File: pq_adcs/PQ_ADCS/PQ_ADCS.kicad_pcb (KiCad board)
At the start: 4 copper layers, 40 x 40 mm, 53 parts, among them IC2 TMUX1108RSVR, IC3 SN74AUP1G08DBVT, J1 LAT, J3 TOP, J4 SLW-110-01-X-S, J5 SLW-110-01-X-S, J6 SLW-110-01-X-S, J7 SLW-110-01-X-S, J8 LAT, J9 LAT, U1 MMC5983MA, U2 LT6005CDHC#TRPBF, U3 PCA9547BS,118, U5 LT6004IMS8#PBF

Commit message: RIP Stefan in NSL
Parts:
- added H1: MountingHole_Pad, MountingHole:MountingHole_3.2mm_M3_Pad, F.Cu at (83.7, 43.3)
- added H2: MountingHole_Pad, MountingHole:MountingHole_3.2mm_M3_Pad, F.Cu at (116.7, 43.3)
- added H3: MountingHole_Pad, MountingHole:MountingHole_3.2mm_M3_Pad, F.Cu at (116.7, 76.3)
- added H4: MountingHole_Pad, MountingHole:MountingHole_3.2mm_M3_Pad, F.Cu at (83.7, 76.3)
- J1: renamed from J7; value SLW-110-01-X-S -> CES-110-02-L-S
- J1, J8, J9: value LAT -> Conn_01x10_MountingPin
- J2: renamed from J4; value SLW-110-01-X-S -> CES-110-02-L-S
- J3: renamed from J6; value SLW-110-01-X-S -> CES-110-02-L-S
- J3: value TOP -> Conn_01x11_MountingPin
- J4: renamed from J5; value SLW-110-01-X-S -> CES-110-02-L-S
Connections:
- C1 pad 1: (no net) -> GND
- C1 pad 2: (no net) -> /VCC
- C10 pad 1: (no net) -> /ph3_ADCS
- C10 pad 2: (no net) -> Net-(C10-Pad2)
- C11 pad 1: (no net) -> /ph4_ADCS
- C11 pad 2: (no net) -> Net-(C11-Pad2)
- C12 pad 1: (no net) -> Net-(C12-Pad1)
- C12 pad 2: (no net) -> /ph6_ADCS
- C13 pad 1: (no net) -> Net-(C13-Pad1)
- C13 pad 2: (no net) -> /ph5_ADCS
- C14 pad 1: (no net) -> /ph_OBC
- C14 pad 2: (no net) -> GND
- C15 pad 1: (no net) -> /VCC
- C15 pad 2: (no net) -> GND
- C16 pad 1: (no net) -> /VCC
- C16 pad 2: (no net) -> GND
- C2 pad 1: (no net) -> GND
- C2 pad 2: (no net) -> Net-(C2-Pad2)
- C3 pad 1: (no net) -> GND
- C3 pad 2: (no net) -> /VCC
- C4 pad 1: (no net) -> GND
- C4 pad 2: (no net) -> /VCC
- C5 pad 1: (no net) -> GND
- C5 pad 2: (no net) -> /VCC
- C6 pad 1: (no net) -> Net-(C6-Pad1)
- C6 pad 2: (no net) -> GND
- C7 pad 1: (no net) -> /VCC
- C7 pad 2: (no net) -> GND
- C8 pad 1: (no net) -> Net-(C8-Pad1)
- C8 pad 2: (no net) -> /ph1_ADCS
- C9 pad 1: (no net) -> Net-(C9-Pad1)
- C9 pad 2: (no net) -> /ph2_ADCS
- IC2 pad 1: (no net) -> /VCC
- IC2 pad 10: (no net) -> GND
- IC2 pad 11: (no net) -> /VCC
- IC2 pad 12: (no net) -> GND
- IC2 pad 13: (no net) -> /SEL_PH2
- IC2 pad 14: (no net) -> /SEL_PH1
- IC2 pad 15: (no net) -> /SEL_PH0
- IC2 pad 16: (no net) -> Net-(IC2-Pad16)
- IC2 pad 2: (no net) -> GND
- IC2 pad 3: (no net) -> /ph2_ADCS
- IC2 pad 4: (no net) -> /ph3_ADCS
- IC2 pad 5: (no net) -> /ph5_ADCS
- IC2 pad 6: (no net) -> /ph_OBC
- IC2 pad 7: (no net) -> /ph4_ADCS
- IC2 pad 8: (no net) -> /ph1_ADCS
- IC2 pad 9: (no net) -> /ph6_ADCS
- IC3 pad 1: (no net) -> /SEL_PH0
- IC3 pad 2: (no net) -> /SEL_PH1
- IC3 pad 3: (no net) -> GND
- IC3 pad 4: (no net) -> Net-(IC2-Pad16)
- IC3 pad 5: (no net) -> /VCC
- J1 pad 1: (no net) -> /SDA
- J1 pad 10: (no net) -> /VCC
- J1 pad 2: (no net) -> /SCL
- J1 pad 3: (no net) -> unconnected-(J7-Pad3)
- J1 pad 4: (no net) -> /BATT++
- J1 pad 5: (no net) -> unconnected-(J7-Pad5)
- J1 pad 6: (no net) -> unconnected-(J7-Pad6)
- J1 pad 7: (no net) -> unconnected-(J7-Pad7)
- J1 pad 8: (no net) -> unconnected-(J7-Pad8)
- J1 pad 9: (no net) -> GND
- J1 pad 1: (no net) -> /SOLAR_X
- J1 pad 10: (no net) -> GND
- J1 pad 2: (no net) -> GND
- J1 pad 3: (no net) -> /Iout6
- J1 pad 4: (no net) -> /VCC
- J1 pad 5: (no net) -> /SDA
- J1 pad 6: (no net) -> /SCL
- J1 pad 7: (no net) -> GND
- J1 pad 8: (no net) -> /pht6
- J1 pad 9: (no net) -> /BURNCOMMS
- J2 pad 1: (no net) -> unconnected-(J4-Pad1)
- J2 pad 10: (no net) -> unconnected-(J4-Pad10)
- J2 pad 2: (no net) -> unconnected-(J4-Pad2)
- J2 pad 3: (no net) -> unconnected-(J4-Pad3)
- J2 pad 4: (no net) -> /SOLAR_Y
- J2 pad 5: (no net) -> /SEL_PH0
- J2 pad 6: (no net) -> /SEL_PH1
- J2 pad 7: (no net) -> unconnected-(J4-Pad7)
- J2 pad 8: (no net) -> unconnected-(J4-Pad8)
- J2 pad 9: (no net) -> /BURNCOMMS
- J3 pad 1: (no net) -> unconnected-(J6-Pad1)
- J3 pad 10: (no net) -> /SOLAR_Z
- J3 pad 2: (no net) -> unconnected-(J6-Pad2)
- J3 pad 3: (no net) -> /VStef
- J3 pad 4: (no net) -> unconnected-(J6-Pad4)
- J3 pad 5: (no net) -> /SEL_PH2
- J3 pad 6: (no net) -> /ph_OBC
- J3 pad 7: (no net) -> /RST_Drivers
- J3 pad 8: (no net) -> unconnected-(J6-Pad8)
- J3 pad 9: (no net) -> unconnected-(J6-Pad9)
- J3 pad 1: (no net) -> /VStef
- J3 pad 10: (no net) -> /Iout1
- J3 pad 11: (no net) -> GND
- J3 pad 2: (no net) -> /SWCLK
- J3 pad 3: (no net) -> /SWDIO
- J3 pad 4: (no net) -> /VCC
- J3 pad 5: (no net) -> /SDA
- J3 pad 6: (no net) -> /SCL
- J3 pad 7: (no net) -> GND
- J3 pad 8: (no net) -> /pht3
- J3 pad 9: (no net) -> GND
- J4 pad 1: (no net) -> unconnected-(J5-Pad1)
- J4 pad 10: (no net) -> /SOLAR_X
- J4 pad 2: (no net) -> unconnected-(J5-Pad2)
- J4 pad 3: (no net) -> unconnected-(J5-Pad3)
- J4 pad 4: (no net) -> /SWCLK
- J4 pad 5: (no net) -> /SWDIO
- J4 pad 6: (no net) -> /NRST
- J4 pad 7: (no net) -> unconnected-(J5-Pad7)
- J4 pad 8: (no net) -> unconnected-(J5-Pad8)
- J4 pad 9: (no net) -> unconnected-(J5-Pad9)
- J8 pad 1: (no net) -> /SOLAR_Z
- J8 pad 10: (no net) -> GND
- J8 pad 2: (no net) -> GND
- J8 pad 3: (no net) -> /Iout5
- J8 pad 4: (no net) -> /VCC
- J8 pad 5: (no net) -> /SDA
- J8 pad 6: (no net) -> /SCL
- J8 pad 7: (no net) -> GND
- J8 pad 8: (no net) -> /pht5
- J8 pad 9: (no net) -> /BURNCOMMS
- J9 pad 1: (no net) -> /SOLAR_Z
- J9 pad 10: (no net) -> GND
- J9 pad 2: (no net) -> GND
- J9 pad 3: (no net) -> /Iout4
- J9 pad 4: (no net) -> /VCC
- J9 pad 5: (no net) -> /SDA
- J9 pad 6: (no net) -> /SCL
- J9 pad 7: (no net) -> GND
- J9 pad 8: (no net) -> /pht1
- J9 pad 9: (no net) -> /BURNCOMMS
- LV1CT1 pad A1: (no net) -> /SCL1
- LV1CT1 pad A2: (no net) -> /NRST
- LV1CT1 pad B1: (no net) -> /SDA1
- LV1CT1 pad B2: (no net) -> /VCC
- LV1CT1 pad C1: (no net) -> GND
- LV1CT1 pad C2: (no net) -> /Iout1
- LV2CT1 pad A1: (no net) -> /SCL2
- LV2CT1 pad A2: (no net) -> /NRST
- LV2CT1 pad B1: (no net) -> /SDA2
- LV2CT1 pad B2: (no net) -> /VCC
- LV2CT1 pad C1: (no net) -> GND
- LV2CT1 pad C2: (no net) -> /Iout2
- LV3CT1 pad A1: (no net) -> /SCL3
- LV3CT1 pad A2: (no net) -> /NRST
- LV3CT1 pad B1: (no net) -> /SDA3
- LV3CT1 pad B2: (no net) -> /VCC
- LV3CT1 pad C1: (no net) -> GND
- LV3CT1 pad C2: (no net) -> /Iout3
- LV4CT1 pad A1: (no net) -> /SCL4
- LV4CT1 pad A2: (no net) -> /NRST
- LV4CT1 pad B1: (no net) -> /SDA4
- LV4CT1 pad B2: (no net) -> /VCC
- LV4CT1 pad C1: (no net) -> GND
- LV4CT1 pad C2: (no net) -> /Iout4
- LV5CT1 pad A1: (no net) -> /SCL5
- LV5CT1 pad A2: (no net) -> /NRST
- LV5CT1 pad B1: (no net) -> /SDA5
- LV5CT1 pad B2: (no net) -> /VCC
- LV5CT1 pad C1: (no net) -> GND
- LV5CT1 pad C2: (no net) -> /Iout5
- LV6CT1 pad A1: (no net) -> /SCL6
- LV6CT1 pad A2: (no net) -> /NRST
- LV6CT1 pad B1: (no net) -> /SDA6
- LV6CT1 pad B2: (no net) -> /VCC
- LV6CT1 pad C1: (no net) -> GND
- LV6CT1 pad C2: (no net) -> /Iout6
- R1 pad 1: (no net) -> /pht1
- R1 pad 2: (no net) -> Net-(C8-Pad1)
- R10 pad 1: (no net) -> Net-(C11-Pad2)
- R10 pad 2: (no net) -> /ph4_ADCS
- R11 pad 1: (no net) -> Net-(C11-Pad2)
- R11 pad 2: (no net) -> /pht4
- R12 pad 1: (no net) -> /ph6_ADCS
- R12 pad 2: (no net) -> Net-(C12-Pad1)
- R13 pad 1: (no net) -> /ph5_ADCS
- R13 pad 2: (no net) -> Net-(C13-Pad1)
- R14 pad 1: (no net) -> Net-(C12-Pad1)
- R14 pad 2: (no net) -> /pht6
- R15 pad 1: (no net) -> Net-(C13-Pad1)
- R15 pad 2: (no net) -> /pht5
- R2 pad 1: (no net) -> /ph1_ADCS
- R2 pad 2: (no net) -> Net-(C8-Pad1)
- R3 pad 1: (no net) -> /VCC
- R3 pad 10: (no net) -> GND
- R3 pad 11: (no net) -> GND
- R3 pad 12: (no net) -> GND
- R3 pad 13: (no net) -> GND
- R3 pad 14: (no net) -> Net-(C2-Pad2)
- R3 pad 15: (no net) -> GND
- R3 pad 16: (no net) -> /VCC
- R3 pad 2: (no net) -> /SCL
- R3 pad 3: (no net) -> /SDA
- R3 pad 4: (no net) -> unconnected-(R3-Pad4)
- R3 pad 5: (no net) -> /VCC
- R3 pad 6: (no net) -> unconnected-(R3-Pad6)
- R3 pad 7: (no net) -> unconnected-(R3-Pad7)
- R3 pad 8: (no net) -> GND
- R3 pad 9: (no net) -> GND
- R4 pad 1: (no net) -> /SCL
- R4 pad 2: (no net) -> /VCC
- R5 pad 1: (no net) -> /VCC
- R5 pad 2: (no net) -> /SDA
- R6 pad 1: (no net) -> /ph2_ADCS
- R6 pad 2: (no net) -> Net-(C9-Pad1)
- R7 pad 1: (no net) -> Net-(C10-Pad2)
- R7 pad 2: (no net) -> /ph3_ADCS
- R8 pad 1: (no net) -> Net-(C10-Pad2)
- R8 pad 2: (no net) -> /pht3
- R9 pad 1: (no net) -> /pht2
- R9 pad 2: (no net) -> Net-(C9-Pad1)
- U1 pad 1: (no net) -> /SCL
- U1 pad 10: (no net) -> Net-(C6-Pad1)
- U1 pad 11: (no net) -> GND
- U1 pad 12: (no net) -> unconnected-(U1-Pad12)
- U1 pad 13: (no net) -> /VCC
- U1 pad 14: (no net) -> unconnected-(U1-Pad14)
- U1 pad 15: (no net) -> unconnected-(U1-Pad15)
- U1 pad 16: (no net) -> /SDA
- U1 pad 2: (no net) -> /VCC
- U1 pad 3: (no net) -> unconnected-(U1-Pad3)
- U1 pad 4: (no net) -> /VCC
- U1 pad 5: (no net) -> unconnected-(U1-Pad5)
- U1 pad 6: (no net) -> unconnected-(U1-Pad6)
- U1 pad 7: (no net) -> unconnected-(U1-Pad7)
- U1 pad 8: (no net) -> unconnected-(U1-Pad8)
- U1 pad 9: (no net) -> GND
- U2 pad 1: (no net) -> /ph1_ADCS
- U2 pad 10: (no net) -> /ph4_ADCS
- U2 pad 11: (no net) -> Net-(C11-Pad2)
- U2 pad 12: (no net) -> GND
- U2 pad 13: (no net) -> GND
- U2 pad 14: (no net) -> GND
- U2 pad 15: (no net) -> Net-(C10-Pad2)
- U2 pad 16: (no net) -> /ph3_ADCS
- U2 pad 17: (no net) -> unconnected-(U2-Pad17)
- U2 pad 2: (no net) -> Net-(C8-Pad1)
- U2 pad 3: (no net) -> GND
- U2 pad 4: (no net) -> /VCC
- U2 pad 5: (no net) -> GND
- U2 pad 6: (no net) -> Net-(C9-Pad1)
- U2 pad 7: (no net) -> /ph2_ADCS
- U2 pad 8: (no net) -> unconnected-(U2-Pad8)
- U2 pad 9: (no net) -> unconnected-(U2-Pad9)
- U3 pad 1: (no net) -> /SDA1
- U3 pad 10: (no net) -> /SDA5
- U3 pad 11: (no net) -> /SCL5
- U3 pad 12: (no net) -> /SDA6
- U3 pad 13: (no net) -> /SCL6
- U3 pad 14: (no net) -> unconnected-(U3-Pad14)
- U3 pad 15: (no net) -> unconnected-(U3-Pad15)
- U3 pad 16: (no net) -> unconnected-(U3-Pad16)
- U3 pad 17: (no net) -> unconnected-(U3-Pad17)
- U3 pad 18: (no net) -> GND
- U3 pad 19: (no net) -> /SCL
- U3 pad 2: (no net) -> /SCL1
- U3 pad 20: (no net) -> /SDA
- U3 pad 21: (no net) -> /VCC
- U3 pad 22: (no net) -> GND
- U3 pad 23: (no net) -> GND
- U3 pad 24: (no net) -> /RST_Drivers
- U3 pad 25: (no net) -> unconnected-(U3-Pad25)
- U3 pad 3: (no net) -> /SDA2
- U3 pad 4: (no net) -> /SCL2
- U3 pad 5: (no net) -> /SDA3
- U3 pad 6: (no net) -> /SCL3
- U3 pad 7: (no net) -> /SDA4
- U3 pad 8: (no net) -> /SCL4
- U3 pad 9: (no net) -> GND
- U5 pad 1: (no net) -> /ph5_ADCS
- U5 pad 2: (no net) -> Net-(C13-Pad1)
- U5 pad 3: (no net) -> GND
- U5 pad 4: (no net) -> GND
- U5 pad 5: (no net) -> GND
- U5 pad 6: (no net) -> Net-(C12-Pad1)
- U5 pad 7: (no net) -> /ph6_ADCS
- U5 pad 8: (no net) -> /VCC
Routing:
- net (no net): track 1529.1 -> 0.00 mm, vias 83 -> 0
- net GND: track 0.00 -> 265.9 mm, vias 0 -> 25
- net /VCC: track 0.00 -> 164.6 mm, vias 0 -> 3
- net /SCL: track 0.00 -> 94.7 mm, vias 0 -> 5
- net /SDA: track 0.00 -> 89.6 mm, vias 0 -> 4
- net /SOLAR_Z: track 0.00 -> 65.7 mm, vias 0 -> 1
- net /BURNCOMMS: track 0.00 -> 60.4 mm, vias 0 -> 2
- net /SOLAR_X: track 0.00 -> 59.8 mm, vias 0 -> 3
- net /Iout5: track 0.00 -> 50.8 mm, vias 0 -> 2
- net /SOLAR_Y: track 0.00 -> 44.7 mm
- net /VStef: track 0.00 -> 44.3 mm, vias 0 -> 1
- net /Iout4: track 0.00 -> 41.8 mm, vias 0 -> 3
- net /NRST: track 0.00 -> 36.7 mm, vias 0 -> 5
- net /Iout6: track 0.00 -> 34.2 mm, vias 0 -> 2
- net /ph3_ADCS: track 0.00 -> 33.4 mm
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
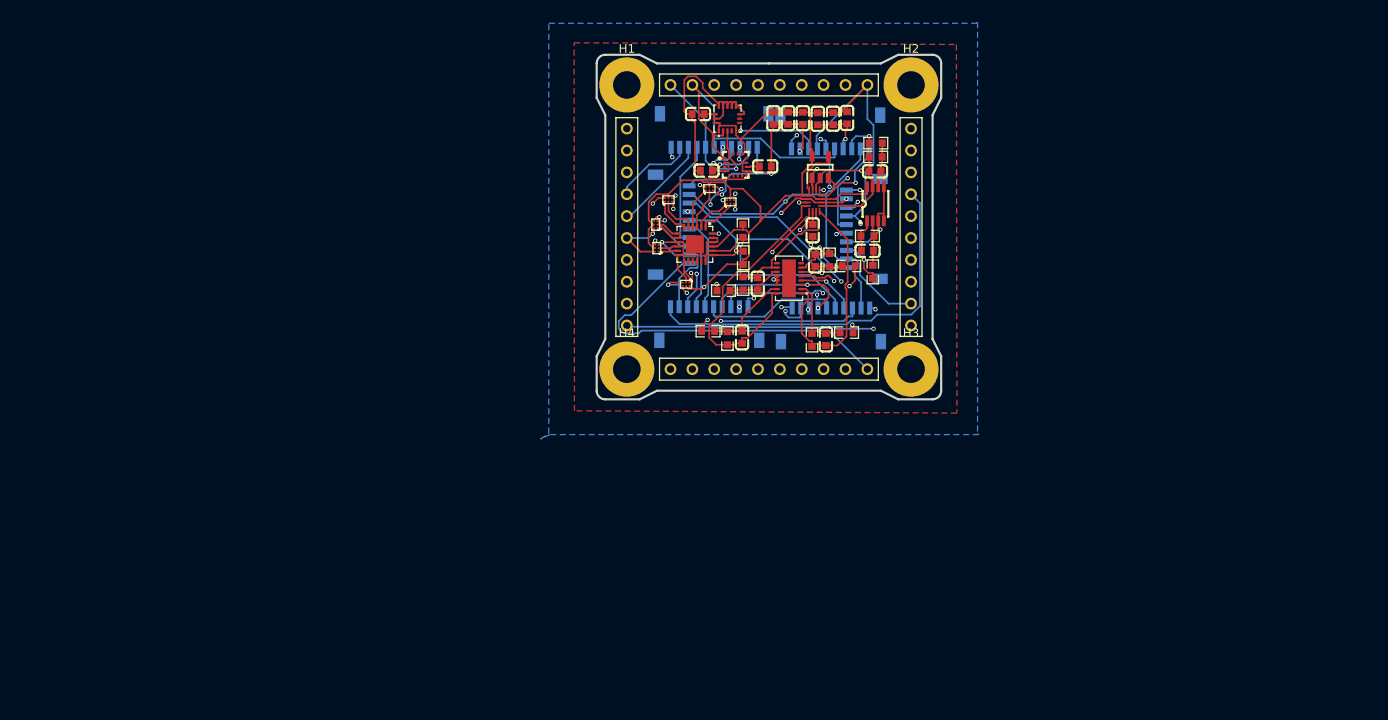
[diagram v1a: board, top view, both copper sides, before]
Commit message: lateral boards added, ADCS schematic lacks mtq drivers
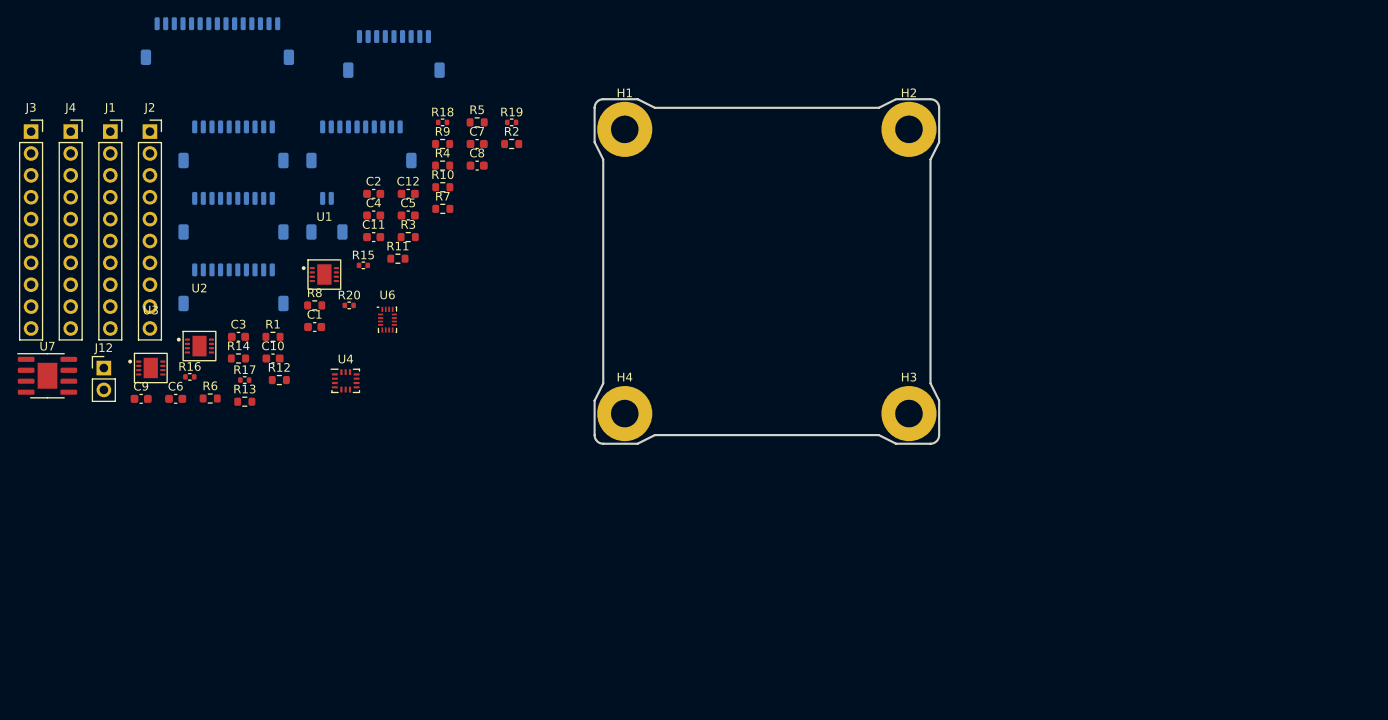
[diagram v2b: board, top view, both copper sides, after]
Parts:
- removed BOT: BOT, easyeda:2023961007
- removed C1: 10nF, easyeda:C0603
- removed C13: 0.1n, easyeda:C0603
- removed C14, C15: 1uF, easyeda:C0603
- removed C16: 1u, easyeda:C0603
- removed the C3 at (105.9, 47.3)
- removed IC2: TMUX1108RSVR, easyeda:QFN40P180X260X55-16N
- removed IC3: SN74AUP1G08DBVT, easyeda:SOT95P280X145-5N
- removed the J1 at (88.8, 43.3)
- removed the J1 at (107.4, 48.1)
- removed the J3 at (88.8, 76.3)
- removed the J3 at (93.9, 47.8)
- removed LAT_: LAT, easyeda:2023961007
- removed LV1CT1, LV2CT1, LV3CT1, LV4CT1, LV5CT1, LV6CT1: LV8498CT_footprint, easyeda:WLP-6_L1.30-W0.90-P0.40-TL
- removed U1: MMC5983MA, easyeda:LGA-16_L3.0-W3.0-P0.50-BL_SQ
- removed the U3 at (91.6, 61.8)
- removed U5: LT6004IMS8#PBF, easyeda:MOSP-8_L3.0-W3.0-P0.65-LS4.9-BL
- added C3: 100 pF, Capacitor_SMD:C_0603_1608Metric, F.Cu at (38.6, 72.6)
- added C3: 100 pF, Capacitor_SMD:C_0603_1608Metric, F.Cu at (47.5, 71.5)
- added J1: CES-110-02-L-S, Connector_PinSocket_2.54mm:PinSocket_1x10_P2.54mm_Vertical, F.Cu at (23.8, 48.8)
- added J10: Pico-Clasp_01x09, Connector_Molex:Molex_Pico-Clasp_202396-0907_1x09-1MP_P1.00mm_Horizontal, B.Cu at (56.7, 39.8)
- added J11: Pico-Clasp_01x15, Connector_Molex:Molex_Pico-Clasp_202396-1507_1x15-1MP_P1.00mm_Horizontal, B.Cu at (36.2, 38.3)
- added J12: CES-102-02-L-S, Connector_PinHeader_2.54mm:PinHeader_1x02_P2.54mm_Vertical, F.Cu at (23.0, 76.2)
- added J3: CES-110-02-L-S, Connector_PinSocket_2.54mm:PinSocket_1x10_P2.54mm_Vertical, F.Cu at (14.6, 48.8)
- added J5: Pico-Clasp_01x02, Connector_Molex:Molex_Pico-Clasp_202396-0207_1x02-1MP_P1.00mm_Horizontal, B.Cu at (48.9, 58.5)
- added J6: Pico-Clasp_01x10, Connector_Molex:Molex_Pico-Clasp_202396-1007_1x10-1MP_P1.00mm_Horizontal, B.Cu at (38.1, 66.8)
- added J7: Pico-Clasp_01x10, Connector_Molex:Molex_Pico-Clasp_202396-1007_1x10-1MP_P1.00mm_Horizontal, B.Cu at (38.1, 58.5)
- added R16: 0R, Resistor_SMD:R_0402_1005Metric, F.Cu at (33.0, 77.2)
- added R17: 0R, Resistor_SMD:R_0402_1005Metric, F.Cu at (39.4, 77.6)
- added R18: 0R, Resistor_SMD:R_0402_1005Metric, F.Cu at (62.4, 47.7)
- added R19: 0R, Resistor_SMD:R_0402_1005Metric, F.Cu at (70.4, 47.7)
- added R20: 0R, Resistor_SMD:R_0402_1005Metric, F.Cu at (51.5, 68.9)
- added U3: LPV542, GGS_Miscellaneous:TI_X1SON-8_3x3mm, F.Cu at (48.6, 65.4)
- added U3: LPV542, GGS_Miscellaneous:TI_X1SON-8_3x3mm, F.Cu at (28.5, 76.2)
- added U4: IIM-42652, Package_LGA:Bosch_LGA-14_3x2.5mm_P0.5mm, F.Cu at (51.1, 77.7)
- added U6: TMUX1108RSVR, GGS_Miscellaneous:UQFN-16_1.8x2.6_Pitch0.4mm, F.Cu at (56.0, 70.6)
- added U7: TCN75AVOA713, Package_SO:SOIC-8-1EP_3.9x4.9mm_P1.27mm_EP2.29x3mm, F.Cu at (16.5, 77.1)
- C10: value 0.1n -> 10 nF; footprint easyeda:C0603 -> Capacitor_SMD:C_0603_1608Metric
- C11, C12, C9: value 0.1n -> 100 nF; footprint easyeda:C0603 -> Capacitor_SMD:C_0603_1608Metric
- C2, C4: value 0.47uF -> 100 pF; footprint easyeda:C0603 -> Capacitor_SMD:C_0603_1608Metric
- C5: value 1uF -> 100 pF; footprint easyeda:C0603 -> Capacitor_SMD:C_0603_1608Metric
- C6: value 10u -> 100 pF; footprint easyeda:C0603 -> Capacitor_SMD:C_0603_1608Metric
- C7: value 0.1u -> 1 uF; footprint easyeda:C0603 -> Capacitor_SMD:C_0603_1608Metric
- C8: value 0.1n -> 2.2 uF; footprint easyeda:C0603 -> Capacitor_SMD:C_0603_1608Metric
- J2, J4: footprint easyeda:SLW-110-01-X-S -> Connector_PinSocket_2.54mm:PinSocket_1x10_P2.54mm_Vertical
- J8, J9: value Conn_01x10_MountingPin -> Pico-Clasp_01x10; footprint easyeda:2023961007 -> Connector_Molex:Molex_Pico-Clasp_202396-1007_1x10-1MP_P1.00mm_Horizontal; moved to B.Cu
- R1, R9: value 100R -> 100; footprint easyeda:R0603 -> Resistor_SMD:R_0603_1608Metric
- R10, R2, R6: value 2k -> 100; footprint easyeda:R0603 -> Resistor_SMD:R_0603_1608Metric
- R11, R8: value 100R -> 2k; footprint easyeda:R0603 -> Resistor_SMD:R_0603_1608Metric
- R12, R7: footprint easyeda:R0603 -> Resistor_SMD:R_0603_1608Metric
- R13: value 2k -> 5k; footprint easyeda:R0603 -> Resistor_SMD:R_0603_1608Metric
- R14: value 100R -> 5k; footprint easyeda:R0603 -> Resistor_SMD:R_0603_1608Metric
- R15: value 100R -> 0R; footprint easyeda:R0603 -> Resistor_SMD:R_0402_1005Metric
- R3: value ICG-20330 -> 2k; footprint easyeda:LGA-16_L3.0-W3.0-P0.50-BL -> Resistor_SMD:R_0603_1608Metric
- R4: value 2.7K -> 2k; footprint easyeda:R0603 -> Resistor_SMD:R_0603_1608Metric
- R5: value 2.7K -> 100; footprint easyeda:R0603 -> Resistor_SMD:R_0603_1608Metric
- U2: value LT6005CDHC#TRPBF -> LPV542; footprint easyeda:DFN-16_L5.0-W3.0-P0.50-BL-EP -> GGS_Miscellaneous:TI_X1SON-8_3x3mm
- moved J2 88.4 mm to (28.4, 48.8), turned to 0 degrees
- moved C9 79.9 mm to (27.4, 79.8), turned to 0 degrees
- moved R14 78.1 mm to (38.6, 75.1), turned to 0 degrees
- moved R13 74.8 mm to (39.4, 80.1)
- moved R12 73.9 mm to (43.4, 77.6)
- moved R6 73.7 mm to (35.4, 79.8), turned to 0 degrees
- moved C6 73.6 mm to (31.4, 79.8)
- moved J9 72.7 mm to (38.1, 50.2), turned to 180 degrees
- moved U2 68.9 mm to (34.1, 73.7), turned to 0 degrees
- moved R1 66.6 mm to (42.7, 72.6), turned to 0 degrees
- moved J4 64.6 mm to (19.2, 48.8), turned to 0 degrees
- moved J8 59.8 mm to (52.9, 50.2), turned to 180 degrees
- moved R15 59.2 mm to (53.1, 64.3), turned to 0 degrees
- moved C4 56.1 mm to (54.4, 58.5), turned to 0 degrees
- moved C10 54.5 mm to (42.7, 75.1), turned to 0 degrees
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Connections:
- net /SOLAR_Z renamed SOLAR_Z
- C10 pad 1: /ph3_ADCS -> 3V3_PERM
- C10 pad 2: Net-(C10-Pad2) -> GND
- C11 pad 1: /ph4_ADCS -> ADCS_POWER
- C11 pad 2: Net-(C11-Pad2) -> GND
- C12 pad 1: Net-(C12-Pad1) -> 3V3_PERM
- C12 pad 2: /ph6_ADCS -> GND
- C2 pad 1: GND -> Net-(C2-Pad1)
- C2 pad 2: Net-(C2-Pad2) -> /PHT2_ADCS
- C4 pad 1: GND -> Net-(C4-Pad1)
- C4 pad 2: /VCC -> /PHT4_ADCS
- C5 pad 1: GND -> /PHT5_ADCS
- C5 pad 2: /VCC -> Net-(C5-Pad2)
- C6 pad 2: GND -> /PHT6_ADCS
- C7 pad 1: /VCC -> 3V3_PERM
- C8 pad 1: Net-(C8-Pad1) -> 3V3_PERM
- C8 pad 2: /ph1_ADCS -> GND
- C9 pad 1: Net-(C9-Pad1) -> 3V3_PERM
- C9 pad 2: /ph2_ADCS -> GND
- J2 pad 1: unconnected-(J4-Pad1) -> STM32_PA15
- J2 pad 10: unconnected-(J4-Pad10) -> GND
- J2 pad 2: unconnected-(J4-Pad2) -> STM32_PB3
- J2 pad 3: unconnected-(J4-Pad3) -> BATT_NTC
- J2 pad 4: /SOLAR_Y -> SOLAR_Y
- J2 pad 5: /SEL_PH0 -> SEL_PH2
- J2 pad 6: /SEL_PH1 -> SEL_PH1
- J2 pad 7: unconnected-(J4-Pad7) -> HEATER_EN
- J2 pad 8: unconnected-(J4-Pad8) -> HEATER_PWR
- J2 pad 9: /BURNCOMMS -> BURNCOMMS
- J4 pad 1: unconnected-(J5-Pad1) -> SOLAR_X
- J4 pad 10: /SOLAR_X -> SCL3
- J4 pad 2: unconnected-(J5-Pad2) -> CHRGOFF
- J4 pad 3: unconnected-(J5-Pad3) -> CLPROG
- J4 pad 4: /SWCLK -> SDA3
- J4 pad 5: /SWDIO -> NRST
- J4 pad 6: /NRST -> SWDIO
- J4 pad 7: unconnected-(J5-Pad7) -> SWCLK
- J4 pad 8: unconnected-(J5-Pad8) -> DAC_PL
- J4 pad 9: unconnected-(J5-Pad9) -> ADC_PL
- J8 pad 10: GND -> BURNCOMMS
- J8 pad 3: /Iout5 -> /MAG-Z
- J8 pad 4: /VCC -> GND
- J8 pad 5: /SDA -> /VCC
- J8 pad 6: /SCL -> /SDA
- J8 pad 7: GND -> /SCL
- J8 pad 8: /pht5 -> /PHT3
- J8 pad 9: /BURNCOMMS -> GND
- J9 pad 10: GND -> BURNCOMMS
- J9 pad 3: /Iout4 -> /MAG+Z
- J9 pad 4: /VCC -> GND
- J9 pad 5: /SDA -> /VCC
- J9 pad 6: /SCL -> /SDA
- J9 pad 7: GND -> /SCL
- J9 pad 8: /pht1 -> /PHT4
- J9 pad 9: /BURNCOMMS -> GND
- R1 pad 1: /pht1 -> /PHT1
- R1 pad 2: Net-(C8-Pad1) -> Net-(C1-Pad2)
- R10 pad 1: Net-(C11-Pad2) -> /PHT6
- R10 pad 2: /ph4_ADCS -> Net-(C6-Pad1)
- R11 pad 1: Net-(C11-Pad2) -> Net-(C5-Pad2)
- R11 pad 2: /pht4 -> /PHT5_ADCS
- R12 pad 1: /ph6_ADCS -> /PHT6_ADCS
- R12 pad 2: Net-(C12-Pad1) -> Net-(C6-Pad1)
- R13 pad 1: /ph5_ADCS -> /SCL
- R13 pad 2: Net-(C13-Pad1) -> 3V3_PERM
- R14 pad 1: Net-(C12-Pad1) -> /SDA
- R14 pad 2: /pht6 -> 3V3_PERM
- R15 pad 1: Net-(C13-Pad1) -> Net-(R15-Pad1)
- R15 pad 2: /pht5 -> 3V3_PERM
- R2 pad 1: /ph1_ADCS -> /PHT2
- R2 pad 2: Net-(C8-Pad1) -> Net-(C2-Pad1)
- R3 pad 1: /VCC -> Net-(C1-Pad2)
- R3 pad 2: /SCL -> /PHT1_ADCS
- R4 pad 1: /SCL -> /PHT2_ADCS
- R4 pad 2: /VCC -> Net-(C2-Pad1)
- R5 pad 1: /VCC -> /PHT3
- R5 pad 2: /SDA -> Net-(C3-Pad2)
- R6 pad 1: /ph2_ADCS -> /PHT4
- R6 pad 2: Net-(C9-Pad1) -> Net-(C4-Pad1)
- R7 pad 1: Net-(C10-Pad2) -> Net-(C3-Pad2)
- R7 pad 2: /ph3_ADCS -> /PHT3_ADCS
- R8 pad 1: Net-(C10-Pad2) -> /PHT4_ADCS
- R8 pad 2: /pht3 -> Net-(C4-Pad1)
- R9 pad 1: /pht2 -> /PHT5
- R9 pad 2: Net-(C9-Pad1) -> Net-(C5-Pad2)
- U2 pad 1: /ph1_ADCS -> /PHT3_ADCS
- U2 pad 2: Net-(C8-Pad1) -> Net-(C3-Pad2)
- U2 pad 4: /VCC -> GND
- U2 pad 5: GND -> 3V3_PERM
- U2 pad 6: Net-(C9-Pad1) -> /PHT4_ADCS
- U2 pad 7: /ph2_ADCS -> Net-(C4-Pad1)
- U2 pad 8: unconnected-(U2-Pad8) -> GND
- U2 pad 9: unconnected-(U2-Pad9) -> GND
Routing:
- net GND: track 265.9 -> 0.00 mm, vias 25 -> 0
- net /VCC: track 164.6 -> 0.00 mm, vias 3 -> 0
- net /SCL: track 94.7 -> 0.00 mm, vias 5 -> 0
- net /SDA: track 89.6 -> 0.00 mm, vias 4 -> 0
- net SOLAR_Z: track 65.7 -> 0.00 mm, vias 1 -> 0
- net /BURNCOMMS: track 60.4 -> 0.00 mm, vias 2 -> 0
- net /SOLAR_X: track 59.8 -> 0.00 mm, vias 3 -> 0
- net /Iout5: track 50.8 -> 0.00 mm, vias 2 -> 0
- net /SOLAR_Y: track 44.7 -> 0.00 mm
- net /VStef: track 44.3 -> 0.00 mm, vias 1 -> 0
- net /Iout4: track 41.8 -> 0.00 mm, vias 3 -> 0
- net /NRST: track 36.7 -> 0.00 mm, vias 5 -> 0
- net /Iout6: track 34.2 -> 0.00 mm, vias 2 -> 0
- net /ph3_ADCS: track 33.4 -> 0.00 mm
- net /ph1_ADCS: track 28.4 -> 0.00 mm
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- removed copper zone on B.Cu, net (none)
- removed copper zone on F.Cu, net (none)
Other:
- outline, holes or cut-outs redrawn
- board text added: "+X"
- board text added: "+Z"
- board text added: "-X"
- board text added: "-Z"
- board text removed: "ADCS-BREAKOUT"

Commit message: designs updated
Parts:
- removed R13, R14: 5k, Resistor_SMD:R_0603_1608Metric
- added C13: 1 uF, Capacitor_SMD:C_0603_1608Metric, F.Cu at (112.0, 73.8)
- added C14: 1 uF, Capacitor_SMD:C_0603_1608Metric, F.Cu at (109.0, 76.8)
- added U5: BD2606MVV, Package_DFN_QFN:QFN-16-1EP_4x4mm_P0.65mm_EP2.5x2.5mm, F.Cu at (108.0, 72.8)
- J12: moved to B.Cu
- moved J3 102.2 mm to (111.4, 81.5), turned to -90 degrees
- moved J2 88.3 mm to (116.5, 53.6)
- moved U7 81.4 mm to (97.8, 72.8), turned to 180 degrees
- moved U3 80.0 mm to (106.5, 58.8), turned to 90 degrees
- moved C6 79.4 mm to (106.5, 54.2)
- moved J12 76.5 mm to (98.7, 65.0), turned to -90 degrees
- moved J7 74.9 mm to (111.8, 71.8), turned to -90 degrees
- moved C9 74.8 mm to (99.0, 58.2), turned to 180 degrees
- moved J11 74.5 mm to (100.0, 76.8)
- moved J4 70.0 mm to (83.5, 76.4), turned to 180 degrees
- moved R12 66.8 mm to (106.5, 55.8), turned to 180 degrees
- moved J1 64.8 mm to (88.6, 48.5), turned to 90 degrees
- moved R6 64.5 mm to (94.0, 52.8), turned to 180 degrees
- moved U2 61.7 mm to (94.0, 58.8), turned to 90 degrees
- moved C10 60.7 mm to (101.8, 61.0), turned to 90 degrees
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- renumbered C3 to C1, U3 to U1
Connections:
- net Net-(R15-Pad1) renamed /TEMP_A0
- net Net-(R17-Pad1) renamed /TEMP_A1
- net Net-(R19-Pad1) renamed /TEMP_A2
- J1 pad 3: UART_TX -> UART_RX
- J10 pad 3: /VCC -> 3V3_PERM
- J10 pad 4: /SDA -> SDA3
- J10 pad 5: /SCL -> SCL3
- J11 pad 15: /V_UMBILICAL -> VCC_UMBILICAL
- J11 pad 5: /VCC -> 3V3_PERM
- J11 pad 6: /SDA -> SDA3
- J11 pad 7: /SCL -> SCL3
- J12 pad 2: ADCS_POWER -> /VCC_MAG
- J6 pad 5: /VCC -> 3V3_PERM
- J6 pad 6: /SDA -> SDA3
- J6 pad 7: /SCL -> SCL3
- J7 pad 5: /VCC -> 3V3_PERM
- J7 pad 6: /SDA -> SDA3
- J7 pad 7: /SCL -> SCL3
- J8 pad 5: /VCC -> 3V3_PERM
- J8 pad 6: /SDA -> SDA3
- J8 pad 7: /SCL -> SCL3
- J9 pad 5: /VCC -> 3V3_PERM
- J9 pad 6: /SDA -> SDA3
- J9 pad 7: /SCL -> SCL3
- U7 pad 1: /SDA -> SDA3
- U7 pad 2: /SCL -> SCL3
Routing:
- net SDA3: track 0.00 -> 37.8 mm
- net BATT-: track 0.00 -> 31.1 mm, vias 0 -> 2
- net 3V3_PERM: track 0.00 -> 27.3 mm, vias 0 -> 4
- net SWCLK: track 0.00 -> 25.5 mm, vias 0 -> 1
- net NRST: track 0.00 -> 23.2 mm, vias 0 -> 1
- net SWDIO: track 0.00 -> 22.5 mm, vias 0 -> 1
- net /PHT5_ADCS: track 0.00 -> 21.9 mm
- net /TEMP_A2: track 0.00 -> 12.3 mm
- net /TEMP_A1: track 0.00 -> 9.89 mm
- net ADCS_POWER: track 0.00 -> 8.29 mm
- net BURNCOMMS: track 0.00 -> 7.77 mm
- net VCC_UMBILICAL: track 0.00 -> 7.04 mm
- net SOLAR_X: track 0.00 -> 6.89 mm
- net /PHT1: track 0.00 -> 6.31 mm, vias 0 -> 1
- net /PHT4_ADCS: track 0.00 -> 6.22 mm, vias 0 -> 1
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- added copper zone on In2.Cu, net 3V3_PERM
- added copper zone on B.Cu, net GND
- added copper zone on F.Cu, net GND
- added copper zone on In1.Cu, net GND
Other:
- board text added: "0"
- board text added: "1"
- board text added: "A0"
- board text added: "A1"
- board text added: "A2"

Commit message: lots of changes
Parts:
- J5: value Pico-Clasp_01x02 -> Conn_01x03_MountingPin; footprint Connector_Molex:Molex_Pico-Clasp_202396-0207_1x02-1MP_P1.00mm_Horizontal -> Connector_Molex:Molex_Pico-Clasp_202396-0307_1x03-1MP_P1.00mm_Horizontal
- moved C7 7.51 mm to (112.8, 63.2), turned to -90 degrees
- moved R9 3.24 mm to (108.8, 62.5), turned to -90 degrees
- moved R10 3.20 mm to (104.2, 55.0), turned to -90 degrees
- moved R2 3.18 mm to (86.5, 55.0), turned to 90 degrees
- moved R6 3.16 mm to (91.8, 55.0), turned to 90 degrees
- moved C8 1.58 mm to (100.6, 56.8), turned to 0 degrees
- moved C9 1.58 mm to (100.6, 58.3), turned to 0 degrees
- moved J10 0.50 mm to (96.8, 53.2)
- moved C11 0.15 mm to (109.2, 78.2)
- moved C13 0.15 mm to (112.0, 73.9)
- moved C14 0.15 mm to (109.2, 76.8)
- moved J7 0.11 mm to (111.7, 71.7)
- moved J5 0.10 mm to (106.2, 53.2)
- moved J8 0.07 mm to (111.7, 58.3)
- turned U6 to -90 degrees
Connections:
- J10 pad 3: 3V3_PERM -> GND
- J10 pad 4: SDA3 -> 3V3_PERM
- J10 pad 5: SCL3 -> SDA3
- J10 pad 6: /PHT6 -> SCL3
- J10 pad 8: BURNCOMMS -> /PHT6
- J10 pad 9: GND -> BURNCOMMS
- J11 pad 2: GND -> /MAG-Y
- J11 pad 3: /MAG-Y -> /VCC_MAG
- J11 pad 4: GND -> 3V3_PERM
- J11 pad 5: 3V3_PERM -> SDA3
- J11 pad 6: SDA3 -> SCL3
- J11 pad 7: SCL3 -> GND
- J12 pad 1: /MAG+Y -> /VCC_MAG
- J12 pad 2: /VCC_MAG -> /MAG+Y
- J2 pad 7: HEATER_EN -> GND
- J6 pad 10: BURNCOMMS -> GND
- J6 pad 2: GND -> /MAG-X
- J6 pad 3: /MAG-X -> /VCC_MAG
- J6 pad 4: GND -> 3V3_PERM
- J6 pad 5: 3V3_PERM -> SDA3
- J6 pad 6: SDA3 -> SCL3
- J6 pad 7: SCL3 -> GND
- J6 pad 9: GND -> BURNCOMMS
- J7 pad 10: BURNCOMMS -> GND
- J7 pad 2: GND -> /MAG+X
- J7 pad 3: /MAG+X -> /VCC_MAG
- J7 pad 4: GND -> 3V3_PERM
- J7 pad 5: 3V3_PERM -> SDA3
- J7 pad 6: SDA3 -> SCL3
- J7 pad 7: SCL3 -> GND
- J7 pad 9: GND -> BURNCOMMS
- J8 pad 10: BURNCOMMS -> GND
- J8 pad 2: GND -> /MAG-Z
- J8 pad 3: /MAG-Z -> /VCC_MAG
- J8 pad 4: GND -> 3V3_PERM
- J8 pad 5: 3V3_PERM -> SDA3
- J8 pad 6: SDA3 -> SCL3
- J8 pad 7: SCL3 -> GND
- J8 pad 9: GND -> BURNCOMMS
- J9 pad 10: BURNCOMMS -> GND
- J9 pad 2: GND -> /MAG+Z
- J9 pad 3: /MAG+Z -> /VCC_MAG
- J9 pad 4: GND -> 3V3_PERM
- J9 pad 5: 3V3_PERM -> SDA3
- J9 pad 6: SDA3 -> SCL3
- J9 pad 7: SCL3 -> GND
- J9 pad 9: GND -> BURNCOMMS
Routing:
- net SCL3: track 0.00 -> 82.8 mm, vias 0 -> 3
- net /PHT1_ADCS: track 4.88 -> 48.7 mm, vias 1 -> 0
- net SDA3: track 37.8 -> 77.2 mm, vias 0 -> 4
- net SEL_PH0: track 0.00 -> 38.0 mm, vias 0 -> 2
- net SOLAR_X: track 6.89 -> 44.3 mm
- net /PHT3_ADCS: track 4.00 -> 39.5 mm, vias 1 -> 0
- net KILLSWITCH+: track 0.00 -> 31.0 mm, vias 0 -> 2
- net ADC_PH: track 0.00 -> 30.1 mm, vias 0 -> 1
- net /PHT2_ADCS: track 6.22 -> 34.0 mm, vias 1 -> 0
- net HEATER_PWR: track 0.00 -> 27.1 mm
- net /MAG+Y: track 0.00 -> 21.1 mm
- net /PHT5: track 0.76 -> 20.1 mm
- net /PHT4_ADCS: track 6.22 -> 25.4 mm, vias 1 -> 0
- net BATT_NTC: track 0.00 -> 14.8 mm, vias 0 -> 1
- net SEL_PH1: track 0.00 -> 12.5 mm
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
